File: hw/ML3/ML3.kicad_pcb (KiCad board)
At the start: 2 copper layers, 125 x 56 mm, 73 parts, among them J1 Conn_01x07, J2 5-12V Supply, J3 Conn_01x20, J4 Conn_01x02, Q1 DMG2305UX-13, SW0 TS04-66-55-BK-160-SMT, T1 Transformer_1P_1S, T2 Transformer_1P_1S, U1 LMV324 (Actually LTV9161), U2 LTV-356T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

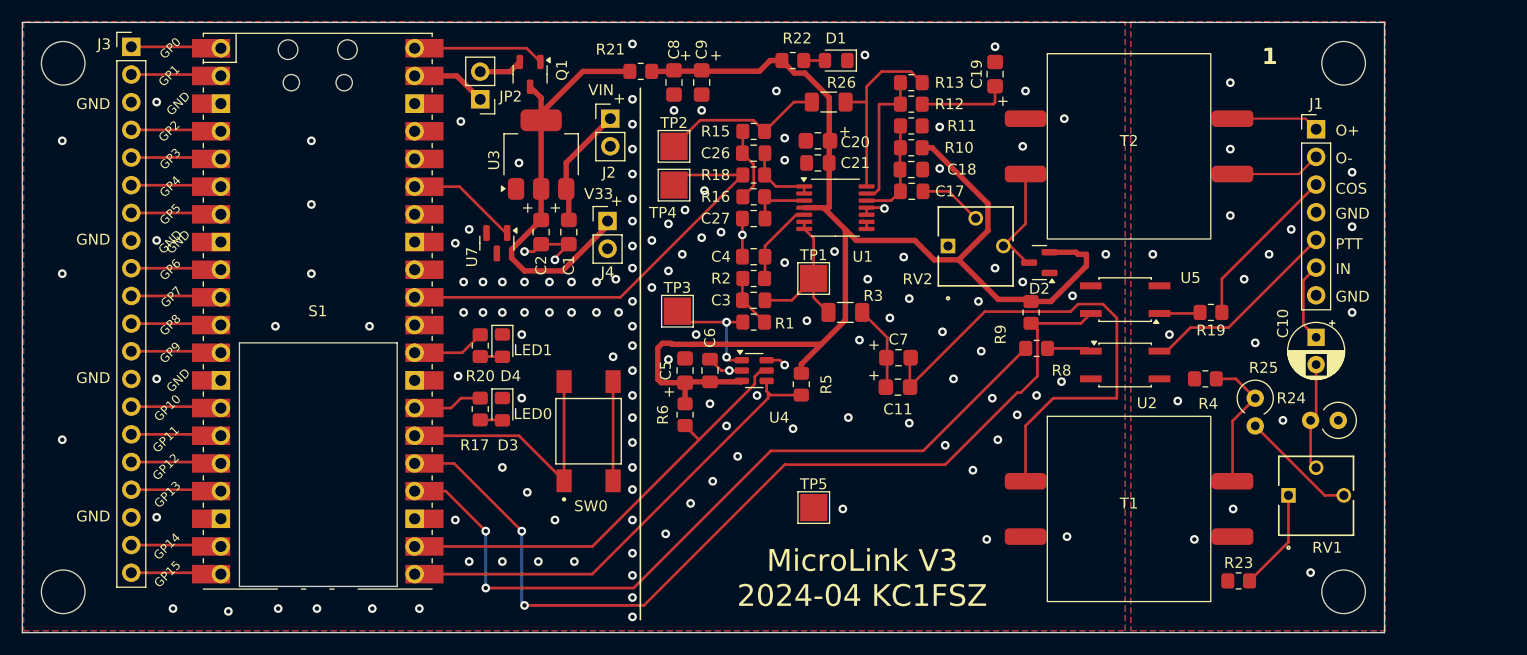
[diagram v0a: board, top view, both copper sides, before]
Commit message: ML3 board modified for improved case/DFM.  Sending this version to Steve
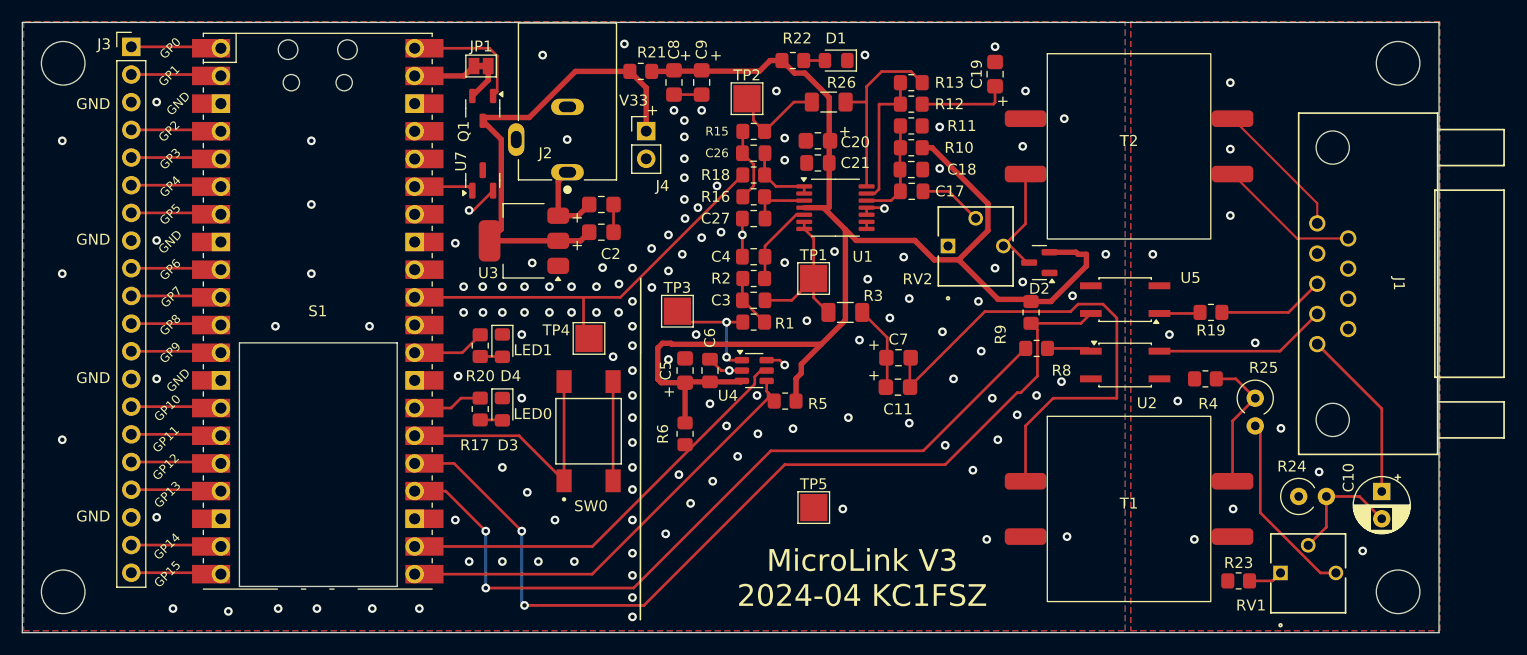
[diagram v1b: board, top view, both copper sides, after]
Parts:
- removed JP2: Jumper_2_Bridged, Connector_PinHeader_2.54mm:PinHeader_1x02_P2.54mm_Vertical
- added JP1: SolderJumper_2_Bridged, Jumper:SolderJumper-2_P1.3mm_Bridged_Pad1.0x1.5mm, F.Cu at (160.1, 48.0)
- J1: value Conn_01x07 -> DE9_Receptacle; footprint Connector_PinHeader_2.54mm:PinHeader_1x07_P2.54mm_Vertical -> bruce-footprints:CONN_A-DF 09 A&slash_KG-T2S_ASM
- J2: value 5-12V Supply -> PJ-102AH; footprint Connector_PinHeader_2.54mm:PinHeader_1x02_P2.54mm_Vertical -> bruce-footprints:Power_5.5mm_CUI_PJ-102AH
- moved J1 18.0 mm to (247.7, 68.0), turned to -90 degrees
- moved TP4 16.1 mm to (170.0, 73.0)
- moved C10 15.4 mm to (242.8, 87.0)
- moved J4 8.98 mm to (175.2, 54.0)
- moved U3 8.07 mm to (164.0, 64.0), turned to 180 degrees
- moved TP2 8.00 mm to (184.5, 51.0)
- moved R24 7.87 mm to (235.1, 87.5), turned to 0 degrees
- moved RV1 7.15 mm to (233.5, 94.5)
- moved U7 5.91 mm to (160.2, 58.5), turned to 90 degrees
- moved C2 5.53 mm to (171.1, 63.2), turned to 0 degrees
- moved Q1 5.35 mm to (160.2, 51.9)
- moved H1 5.00 mm to (244.2, 96.2)
- moved H2 5.00 mm to (244.2, 47.8)
- moved J2 4.24 mm to (168.0, 51.2), turned to 90 degrees
- moved C1 3.92 mm to (171.1, 60.7), turned to 0 degrees
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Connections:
- J1 pad 1: RIG_AF_OUT+ -> RIG_AF_IN
- J1 pad 2: RIG_AF_OUT- -> RIG_PTT
- J1 pad 4: RIG_GND -> unconnected-(J1-Pad4)
- J1 pad 5: RIG_PTT -> RIG_AF_OUT+
- J1 pad 6: RIG_AF_IN -> RIG_GND
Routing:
- net RIG_AF_IN: track 7.37 -> 16.0 mm
- net Net-(R25-Pad2): track 10.8 -> 17.4 mm
- net Net-(R23-Pad2): track 9.33 -> 3.15 mm
- net Net-(R15-Pad2): track 14.7 -> 8.67 mm
- net RIG_COS: track 15.3 -> 9.84 mm
- net Net-(S1-ADC_VREF): track 10.3 -> 5.45 mm
- net RIG_AF_OUT+: track 8.07 -> 12.8 mm
- net RIG_AF_OUT-: track 8.32 -> 13.1 mm
- net +3.3V: track 39.2 -> 43.8 mm
- net +3.3VA: track 123.1 -> 127.6 mm
- net +5VA: track 11.4 -> 8.18 mm
- net I2C0_SDA: track 43.9 -> 41.1 mm
- net ADC0: track 41.5 -> 38.7 mm
- net RIG_PTT: track 18.6 -> 15.9 mm
- net I2C0_SCL: track 41.2 -> 39.4 mm
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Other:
- board size 125 x 56 mm -> 130 x 56 mm
- board text added: "J1: Radio connection (DB9)"
- board text added: "J2: DC Power Connection (5.5mm)"
- board text removed: "1"
- board text removed: "COS"
- board text removed: "IN"
- board text removed: "J1: Radio connection (via DB9)"
- board text removed: "J2: DC Power Connection"
- board text removed: "O+"
- board text removed: "O-"
- board text removed: "PTT"
- board text removed: "VIN"
